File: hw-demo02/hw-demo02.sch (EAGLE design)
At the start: 14 parts, among them Q1 BTS500101TADATMA2

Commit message: removed unused traces and vias, layout tweaks
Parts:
- removed J_IS: 0R0, rcl:R-US_0207/12
- added TP_VS: 22-23-2021, con-molex:22-23-2021
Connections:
- removed net N$2: J_IS.2, R_IS.1, TP_IS-1.S, TP_IS-2.S
- net IS: now also R_IS.1; no longer J_IS.1
- net IS_OUT: now also TP_IS-1.S, TP_IS-2.S
- net VS_OUT: now also TP_VS-1.S, TP_VS-2.S
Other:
- moved on the sheet: R_IS
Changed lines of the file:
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@@
 <part name="R_ISPD" library="rcl" deviceset="R-US_" device="0207/12" value="1K0"/>
 <part name="GND14" library="supply1" deviceset="GND" device=""/>
-<part name="J_IS" library="rcl" deviceset="R-US_" device="0207/12" value="0R0"/>
+<part name="R_IS" library="rcl" deviceset="R-US_" device="0207/12" value="10K"/>
 <part name="TP_IS" library="con-molex" deviceset="22-23-2021" device="" value=""/>
 <part name="TP_IN" library="con-molex" deviceset="22-23-2021" device="" value=""/>
 <part name="R_GND" library="rcl" deviceset="R-US_" device="R1206W" value="0R0"/>
-<part name="R_IS" library="rcl" deviceset="R-US_" device="0207/12" value="10K"/>
 <part name="Q1" library="BTS500101TADATMA2" deviceset="BTS500101TADATMA2" device="" value=""/>
 <part name="P+8" library="supply1" deviceset="+12V" device=""/>
 <part name="GND15" library="supply1" deviceset="GND" device=""/>
 <part name="C_VS" library="rcl" deviceset="C-US" device="C0805K" value="100n"/>
+<part name="TP_VS" library="con-molex" deviceset="22-23-2021" device="" value=""/>
 </parts>
 <sheets>
@@
 <instance part="R_ISPD" gate="G$1" x="195.58" y="142.24" rot="R90"/>
 <instance part="GND14" gate="1" x="195.58" y="127"/>
-<instance part="J_IS" gate="G$1" x="177.8" y="157.48" rot="R180"/>
+<instance part="R_IS" gate="G$1" x="177.8" y="157.48" rot="R180"/>
 <instance part="TP_IS" gate="-1" x="167.64" y="149.86"/>
 <instance part="TP_IS" gate="-2" x="167.64" y="147.32"/>
@@
 <instance part="TP_IN" gate="-2" x="160.02" y="170.18"/>
 <instance part="R_GND" gate="G$1" x="205.74" y="180.34"/>
-<instance part="R_IS" gate="G$1" x="144.78" y="157.48" rot="R180"/>
 <instance part="Q1" gate="G$1" x="215.9" y="162.56"/>
 <instance part="P+8" gate="1" x="251.46" y="175.26"/>
 <instance part="GND15" gate="1" x="251.46" y="147.32"/>
 <instance part="C_VS" gate="G$1" x="251.46" y="157.48"/>
+<instance part="TP_VS" gate="-1" x="93.98" y="137.16"/>
+<instance part="TP_VS" gate="-2" x="93.98" y="137.16"/>
 </instances>
 <busses>
@@
 <wire x1="76.2" y1="127" x2="76.2" y2="129.54" width="0.1524" layer="91"/>
 <wire x1="76.2" y1="129.54" x2="76.2" y2="134.62" width="0.1524" layer="91"/>
-<wire x1="86.36" y1="129.54" x2="76.2" y2="129.54" width="0.1524" layer="91"/>
+<wire x1="106.68" y1="129.54" x2="88.9" y2="129.54" width="0.1524" layer="91"/>
 <junction x="76.2" y="129.54"/>
-<label x="86.36" y="129.54" size="1.27" layer="95" xref="yes"/>
+<label x="106.68" y="129.54" size="1.27" layer="95" xref="yes"/>
+<wire x1="88.9" y1="129.54" x2="76.2" y2="129.54" width="0.1524" layer="91"/>
+<wire x1="88.9" y1="129.54" x2="88.9" y2="137.16" width="0.1524" layer="91"/>
+<junction x="88.9" y="129.54"/>
+<pinref part="TP_VS" gate="-1" pin="S"/>
+<pinref part="TP_VS" gate="-2" pin="S"/>
+<wire x1="88.9" y1="137.16" x2="91.44" y2="137.16" width="0.1524" layer="91"/>
+<junction x="91.44" y="137.16"/>
 </segment>
 <segment>
@@
 <wire x1="195.58" y1="157.48" x2="182.88" y2="157.48" width="0.1524" layer="91"/>
 <junction x="195.58" y="157.48"/>
-<pinref part="J_IS" gate="G$1" pin="1"/>
+<pinref part="R_IS" gate="G$1" pin="1"/>
 <pinref part="Q1" gate="G$1" pin="IS"/>
 <wire x1="195.58" y1="157.48" x2="215.9" y2="157.48" width="0.1524" layer="91"/>
@@
 <segment>
 <label x="132.08" y="157.48" size="1.27" layer="95" rot="R180" xref="yes"/>
-<pinref part="R_IS" gate="G$1" pin="2"/>
-<wire x1="139.7" y1="157.48" x2="132.08" y2="157.48" width="0.1524" layer="91"/>
-</segment>
-<segment>
-<pinref part="CONTROL" gate="G$1" pin="3"/>
-<wire x1="228.6" y1="78.74" x2="231.14" y2="78.74" width="0.1524" layer="91"/>
-<label x="228.6" y="78.74" size="1.27" layer="95" rot="R180" xref="yes"/>
-</segment>
-</net>
-<net name="N$2" class="0">
-<segment>
 <pinref part="TP_IS" gate="-2" pin="S"/>
 <pinref part="TP_IS" gate="-1" pin="S"/>
 <wire x1="165.1" y1="149.86" x2="165.1" y2="147.32" width="0.1524" layer="91"/>
-<pinref part="R_IS" gate="G$1" pin="1"/>
-<pinref part="J_IS" gate="G$1" pin="2"/>
-<wire x1="149.86" y1="157.48" x2="165.1" y2="157.48" width="0.1524" layer="91"/>
+<pinref part="R_IS" gate="G$1" pin="2"/>
 <wire x1="165.1" y1="157.48" x2="172.72" y2="157.48" width="0.1524" layer="91"/>
 <wire x1="165.1" y1="149.86" x2="165.1" y2="157.48" width="0.1524" layer="91"/>
 <junction x="165.1" y="149.86"/>
 <junction x="165.1" y="157.48"/>
-</segment>
-</net>
+<wire x1="132.08" y1="157.48" x2="165.1" y2="157.48" width="0.1524" layer="91"/>
+</segment>
+<segment>
+<pinref part="CONTROL" gate="G$1" pin="3"/>
+<wire x1="228.6" y1="78.74" x2="231.14" y2="78.74" width="0.1524" layer="91"/>
+<label x="228.6" y="78.74" size="1.27" layer="95" rot="R180" xref="yes"/>
+</segment>
+</net>

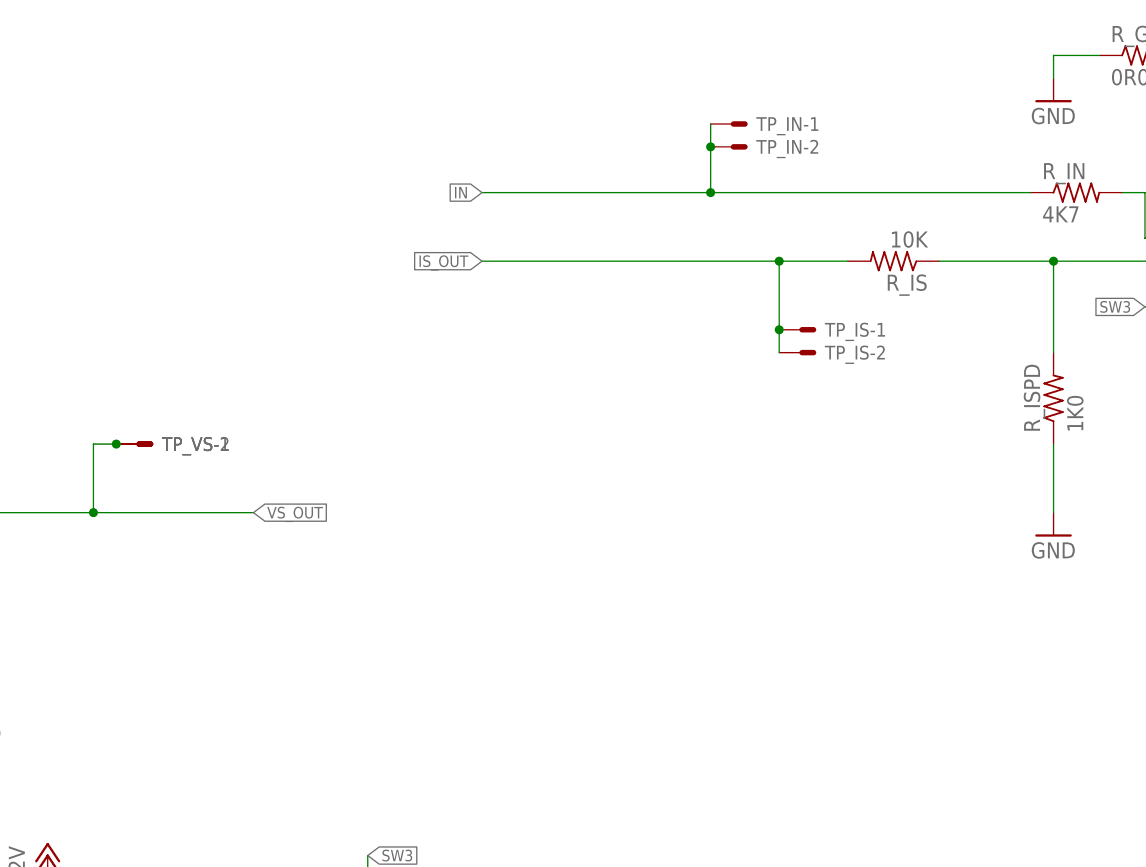
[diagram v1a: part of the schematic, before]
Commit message: layout tweaks and layer stitching, added ground test point
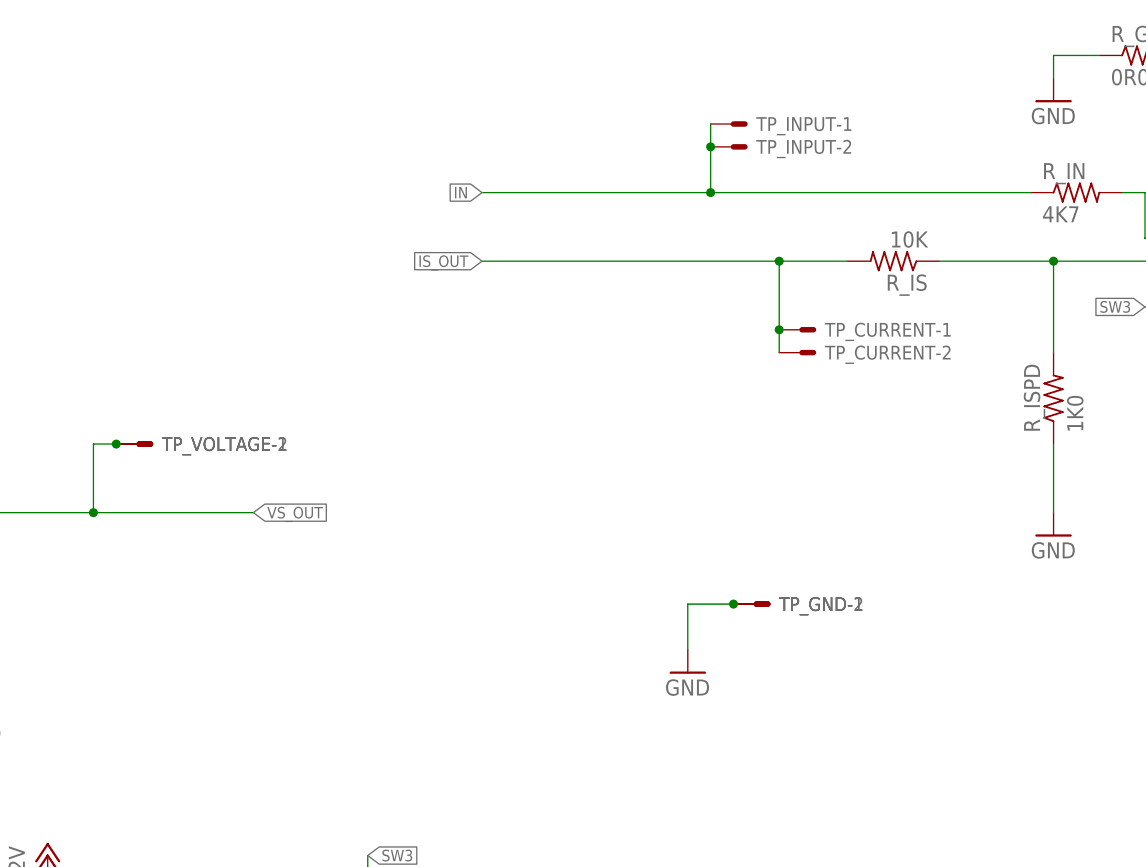
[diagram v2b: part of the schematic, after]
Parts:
- added TP_GND: 22-23-2021, con-molex:22-23-2021
- renumbered TP_IN to TP_INPUT, TP_IS to TP_CURRENT, TP_VS to TP_VOLTAGE
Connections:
- net GND: now also TP_GND-1.S, TP_GND-2.S
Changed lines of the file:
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@@
 <grid distance="0.1" unitdist="inch" unit="inch" style="lines" multiple="1" display="no" altdistance="0.01" altunitdist="inch" altunit="inch"/>
 <layers>
-<layer number="1" name="Top" color="4" fill="1" visible="yes" active="no"/>
-<layer number="16" name="Bottom" color="1" fill="1" visible="yes" active="no"/>
-<layer number="17" name="Pads" color="2" fill="1" visible="yes" active="no"/>
-<layer number="18" name="Vias" color="2" fill="1" visible="yes" active="no"/>
-<layer number="19" name="Unrouted" color="6" fill="1" visible="yes" active="no"/>
-<layer number="20" name="Dimension" color="15" fill="1" visible="yes" active="no"/>
-<layer number="21" name="tPlace" color="7" fill="1" visible="yes" active="no"/>
-<layer number="22" name="bPlace" color="7" fill="1" visible="yes" active="no"/>
-<layer number="23" name="tOrigins" color="15" fill="1" visible="yes" active="no"/>
-<layer number="24" name="bOrigins" color="15" fill="1" visible="yes" active="no"/>
-<layer number="25" name="tNames" color="7" fill="1" visible="yes" active="no"/>
-<layer number="26" name="bNames" color="7" fill="1" visible="yes" active="no"/>
-<layer number="27" name="tValues" color="7" fill="1" visible="yes" active="no"/>
-<layer number="28" name="bValues" color="7" fill="1" visible="yes" active="no"/>
+<layer number="1" name="Top" color="4" fill="1" visible="no" active="no"/>
+<layer number="16" name="Bottom" color="1" fill="1" visible="no" active="no"/>
+<layer number="17" name="Pads" color="2" fill="1" visible="no" active="no"/>
+<layer number="18" name="Vias" color="2" fill="1" visible="no" active="no"/>
+<layer number="19" name="Unrouted" color="6" fill="1" visible="no" active="no"/>
+<layer number="20" name="Dimension" color="15" fill="1" visible="no" active="no"/>
+<layer number="21" name="tPlace" color="7" fill="1" visible="no" active="no"/>
+<layer number="22" name="bPlace" color="7" fill="1" visible="no" active="no"/>
+<layer number="23" name="tOrigins" color="15" fill="1" visible="no" active="no"/>
+<layer number="24" name="bOrigins" color="15" fill="1" visible="no" active="no"/>
+<layer number="25" name="tNames" color="7" fill="1" visible="no" active="no"/>
+<layer number="26" name="bNames" color="7" fill="1" visible="no" active="no"/>
+<layer number="27" name="tValues" color="7" fill="1" visible="no" active="no"/>
+<layer number="28" name="bValues" color="7" fill="1" visible="no" active="no"/>
 <layer number="29" name="tStop" color="7" fill="3" visible="no" active="no"/>
 <layer number="30" name="bStop" color="7" fill="6" visible="no" active="no"/>
@@
 <layer number="35" name="tGlue" color="7" fill="4" visible="no" active="no"/>
 <layer number="36" name="bGlue" color="7" fill="5" visible="no" active="no"/>
-<layer number="37" name="tTest" color="7" fill="1" visible="yes" active="no"/>
-<layer number="38" name="bTest" color="7" fill="1" visible="yes" active="no"/>
+<layer number="37" name="tTest" color="7" fill="1" visible="no" active="no"/>
+<layer number="38" name="bTest" color="7" fill="1" visible="no" active="no"/>
 <layer number="39" name="tKeepout" color="4" fill="11" visible="no" active="no"/>
 <layer number="40" name="bKeepout" color="1" fill="11" visible="no" active="no"/>
@@
 <layer number="44" name="Drills" color="7" fill="1" visible="no" active="no"/>
 <layer number="45" name="Holes" color="7" fill="1" visible="no" active="no"/>
-<layer number="46" name="Milling" color="3" fill="1" visible="yes" active="no"/>
-<layer number="47" name="Measures" color="7" fill="1" visible="yes" active="no"/>
-<layer number="48" name="Document" color="7" fill="1" visible="yes" active="no"/>
-<layer number="49" name="Reference" color="7" fill="1" visible="yes" active="no"/>
-<layer number="50" name="dxf" color="7" fill="1" visible="yes" active="no"/>
-<layer number="51" name="tDocu" color="7" fill="1" visible="yes" active="no"/>
-<layer number="52" name="bDocu" color="7" fill="1" visible="yes" active="no"/>
-<layer number="53" name="tGND_GNDA" color="7" fill="9" visible="yes" active="no"/>
-<layer number="54" name="bGND_GNDA" color="1" fill="9" visible="yes" active="no"/>
-<layer number="56" name="wert" color="7" fill="1" visible="yes" active="no"/>
-<layer number="57" name="tCAD" color="7" fill="1" visible="yes" active="no"/>
-<layer number="59" name="tCarbon" color="7" fill="1" visible="yes" active="no"/>
-<layer number="60" name="bCarbon" color="7" fill="1" visible="yes" active="no"/>
+<layer number="46" name="Milling" color="3" fill="1" visible="no" active="no"/>
+<layer number="47" name="Measures" color="7" fill="1" visible="no" active="no"/>
+<layer number="48" name="Document" color="7" fill="1" visible="no" active="no"/>
+<layer number="49" name="Reference" color="7" fill="1" visible="no" active="no"/>
+<layer number="50" name="dxf" color="7" fill="1" visible="no" active="no"/>
+<layer number="51" name="tDocu" color="7" fill="1" visible="no" active="no"/>
+<layer number="52" name="bDocu" color="7" fill="1" visible="no" active="no"/>
+<layer number="53" name="tGND_GNDA" color="7" fill="9" visible="no" active="no"/>
+<layer number="54" name="bGND_GNDA" color="1" fill="9" visible="no" active="no"/>
+<layer number="56" name="wert" color="7" fill="1" visible="no" active="no"/>
+<layer number="57" name="tCAD" color="7" fill="1" visible="no" active="no"/>
+<layer number="59" name="tCarbon" color="7" fill="1" visible="no" active="no"/>
+<layer number="60" name="bCarbon" color="7" fill="1" visible="no" active="no"/>
 <layer number="90" name="Modules" color="5" fill="1" visible="yes" active="yes"/>
 <layer number="91" name="Nets" color="2" fill="1" visible="yes" active="yes"/>
@@
 <part name="GND14" library="supply1" deviceset="GND" device=""/>
 <part name="R_IS" library="rcl" deviceset="R-US_" device="0207/12" value="10K"/>
-<part name="TP_IS" library="con-molex" deviceset="22-23-2021" device="" value=""/>
-<part name="TP_IN" library="con-molex" deviceset="22-23-2021" device="" value=""/>
+<part name="TP_CURRENT" library="con-molex" deviceset="22-23-2021" device="" value=""/>
+<part name="TP_INPUT" library="con-molex" deviceset="22-23-2021" device="" value=""/>
 <part name="R_GND" library="rcl" deviceset="R-US_" device="R1206W" value="0R0"/>
 <part name="Q1" library="BTS500101TADATMA2" deviceset="BTS500101TADATMA2" device="" value=""/>
@@
 <part name="GND15" library="supply1" deviceset="GND" device=""/>
 <part name="C_VS" library="rcl" deviceset="C-US" device="C0805K" value="100n"/>
-<part name="TP_VS" library="con-molex" deviceset="22-23-2021" device="" value=""/>
+<part name="TP_VOLTAGE" library="con-molex" deviceset="22-23-2021" device="" value=""/>
+<part name="TP_GND" library="con-molex" deviceset="22-23-2021" device="" value=""/>
+<part name="GND1" library="supply1" deviceset="GND" device=""/>
 </parts>
 <sheets>
@@
 <instance part="GND14" gate="1" x="195.58" y="127"/>
 <instance part="R_IS" gate="G$1" x="177.8" y="157.48" rot="R180"/>
-<instance part="TP_IS" gate="-1" x="167.64" y="149.86"/>
-<instance part="TP_IS" gate="-2" x="167.64" y="147.32"/>
-<instance part="TP_IN" gate="-1" x="160.02" y="172.72"/>
-<instance part="TP_IN" gate="-2" x="160.02" y="170.18"/>
+<instance part="TP_CURRENT" gate="-1" x="167.64" y="149.86"/>
+<instance part="TP_CURRENT" gate="-2" x="167.64" y="147.32"/>
+<instance part="TP_INPUT" gate="-1" x="160.02" y="172.72"/>
+<instance part="TP_INPUT" gate="-2" x="160.02" y="170.18"/>
 <instance part="R_GND" gate="G$1" x="205.74" y="180.34"/>
 <instance part="Q1" gate="G$1" x="215.9" y="162.56"/>
@@
 <instance part="GND15" gate="1" x="251.46" y="147.32"/>
 <instance part="C_VS" gate="G$1" x="251.46" y="157.48"/>
-<instance part="TP_VS" gate="-1" x="93.98" y="137.16"/>
-<instance part="TP_VS" gate="-2" x="93.98" y="137.16"/>
+<instance part="TP_VOLTAGE" gate="-1" x="93.98" y="137.16"/>
+<instance part="TP_VOLTAGE" gate="-2" x="93.98" y="137.16"/>
+<instance part="TP_GND" gate="-1" x="162.56" y="119.38"/>
+<instance part="TP_GND" gate="-2" x="162.56" y="119.38"/>
+<instance part="GND1" gate="1" x="154.94" y="111.76"/>
 </instances>
 <busses>
@@
 <wire x1="251.46" y1="152.4" x2="251.46" y2="149.86" width="0.1524" layer="91"/>
 </segment>
+<segment>
+<pinref part="GND1" gate="1" pin="GND"/>
+<wire x1="154.94" y1="114.3" x2="154.94" y2="119.38" width="0.1524" layer="91"/>
+<pinref part="TP_GND" gate="-1" pin="S"/>
+<pinref part="TP_GND" gate="-2" pin="S"/>
+<wire x1="154.94" y1="119.38" x2="160.02" y2="119.38" width="0.1524" layer="91"/>
+<junction x="160.02" y="119.38"/>
+</segment>
 </net>
 <net name="+12V" class="0">
@@
 <wire x1="132.08" y1="165.1" x2="157.48" y2="165.1" width="0.1524" layer="91"/>
 <label x="132.08" y="165.1" size="1.27" layer="95" rot="R180" xref="yes"/>
-<pinref part="TP_IN" gate="-1" pin="S"/>
-<pinref part="TP_IN" gate="-2" pin="S"/>
+<pinref part="TP_INPUT" gate="-1" pin="S"/>
+<pinref part="TP_INPUT" gate="-2" pin="S"/>
 <wire x1="157.48" y1="165.1" x2="193.04" y2="165.1" width="0.1524" layer="91"/>
 <wire x1="157.48" y1="172.72" x2="157.48" y2="170.18" width="0.1524" layer="91"/>
@@
 <wire x1="88.9" y1="129.54" x2="88.9" y2="137.16" width="0.1524" layer="91"/>
 <junction x="88.9" y="129.54"/>
-<pinref part="TP_VS" gate="-1" pin="S"/>
-<pinref part="TP_VS" gate="-2" pin="S"/>
+<pinref part="TP_VOLTAGE" gate="-1" pin="S"/>
+<pinref part="TP_VOLTAGE" gate="-2" pin="S"/>
 <wire x1="88.9" y1="137.16" x2="91.44" y2="137.16" width="0.1524" layer="91"/>
 <junction x="91.44" y="137.16"/>
@@
 <segment>
 <label x="132.08" y="157.48" size="1.27" layer="95" rot="R180" xref="yes"/>
-<pinref part="TP_IS" gate="-2" pin="S"/>
-<pinref part="TP_IS" gate="-1" pin="S"/>
+<pinref part="TP_CURRENT" gate="-2" pin="S"/>
+<pinref part="TP_CURRENT" gate="-1" pin="S"/>
 <wire x1="165.1" y1="149.86" x2="165.1" y2="147.32" width="0.1524" layer="91"/>
 <pinref part="R_IS" gate="G$1" pin="2"/>

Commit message: layout refinement
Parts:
- renumbered TP_VOLTAGE to TP_VDIV
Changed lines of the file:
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@@
 <part name="GND15" library="supply1" deviceset="GND" device=""/>
 <part name="C_VS" library="rcl" deviceset="C-US" device="C0805K" value="100n"/>
-<part name="TP_VOLTAGE" library="con-molex" deviceset="22-23-2021" device="" value=""/>
+<part name="TP_VDIV" library="con-molex" deviceset="22-23-2021" device="" value=""/>
 <part name="TP_GND" library="con-molex" deviceset="22-23-2021" device="" value=""/>
 <part name="GND1" library="supply1" deviceset="GND" device=""/>
@@
 <instance part="GND15" gate="1" x="251.46" y="147.32"/>
 <instance part="C_VS" gate="G$1" x="251.46" y="157.48"/>
-<instance part="TP_VOLTAGE" gate="-1" x="93.98" y="137.16"/>
-<instance part="TP_VOLTAGE" gate="-2" x="93.98" y="137.16"/>
+<instance part="TP_VDIV" gate="-1" x="93.98" y="137.16"/>
+<instance part="TP_VDIV" gate="-2" x="93.98" y="137.16"/>
 <instance part="TP_GND" gate="-1" x="162.56" y="119.38"/>
 <instance part="TP_GND" gate="-2" x="162.56" y="119.38"/>
@@
 <wire x1="88.9" y1="129.54" x2="88.9" y2="137.16" width="0.1524" layer="91"/>
 <junction x="88.9" y="129.54"/>
-<pinref part="TP_VOLTAGE" gate="-1" pin="S"/>
-<pinref part="TP_VOLTAGE" gate="-2" pin="S"/>
+<pinref part="TP_VDIV" gate="-1" pin="S"/>
+<pinref part="TP_VDIV" gate="-2" pin="S"/>
 <wire x1="88.9" y1="137.16" x2="91.44" y2="137.16" width="0.1524" layer="91"/>
 <junction x="91.44" y="137.16"/>
